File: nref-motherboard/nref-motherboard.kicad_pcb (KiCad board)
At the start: 2 copper layers, 110 x 80 mm, 137 parts, among them J1 POWSW, J10 Conn_01x20_Pin, J2 USB_C_Receptacle_USB2.0, J3 USBSEL, J4 1-2199230-6, J5 SYSCTL, J6 USB_INT1, J7 CHARGER, J8 Conn_01x12_Pin, J9 Conn_01x14_Pin, Q1 NTMFD6H840NL, Q2 NTMFD6H840NL, SW1 SW_DIP_x01, SW2 RESET, U1 reform2-som-connector, U2 74HC573, U3 MAX1837EUT33+T, U4 TLV1117-18, U5 TPS5450DDAR, U6 TPS5450DDAR, U7 LM2830XQMFE/NOPB, U8 RP2040, U9 W25Q32JVSS, Y1 12MHz 18pF

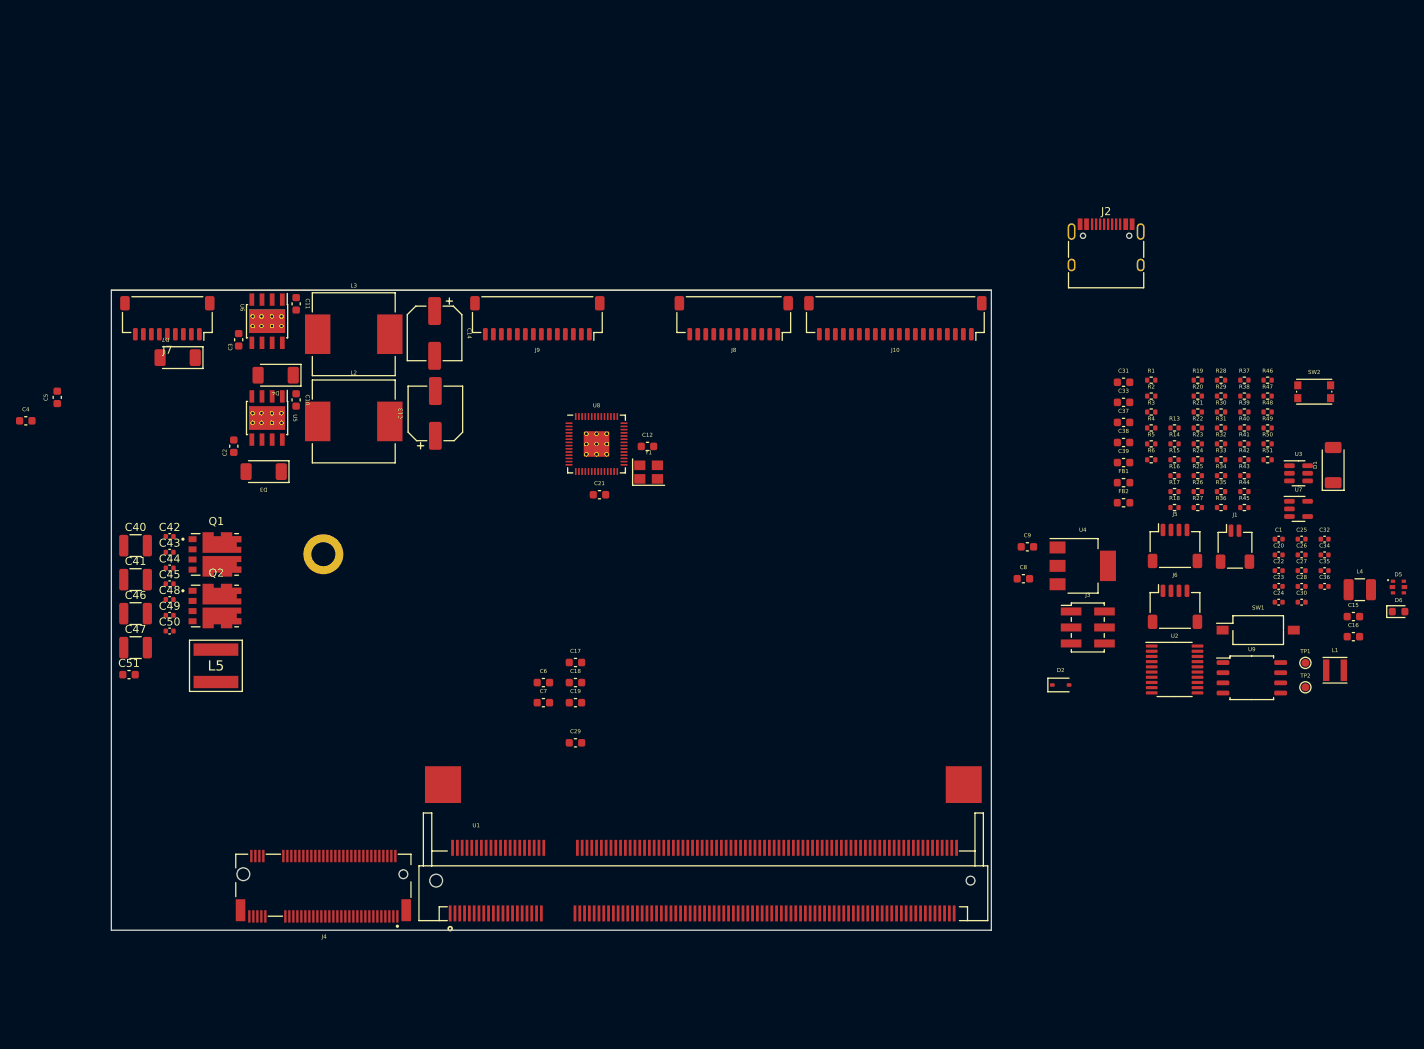
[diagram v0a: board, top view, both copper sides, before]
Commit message: motherboard: upgrade bucks to lm62460; some power layout
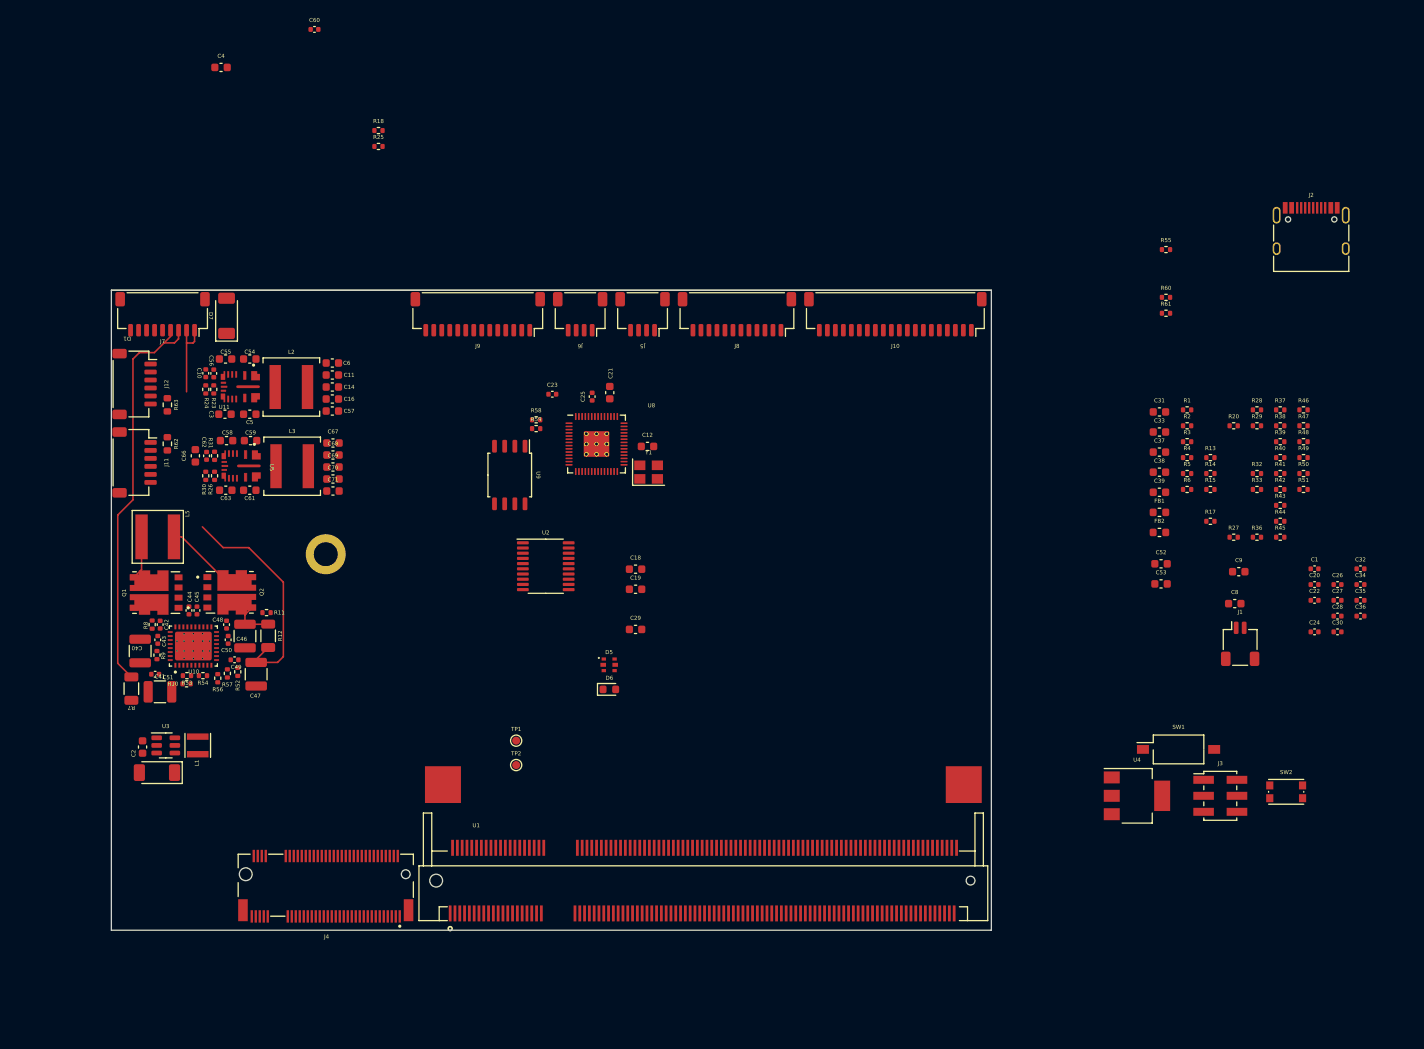
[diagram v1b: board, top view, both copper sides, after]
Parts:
- removed C13: 330uF, Capacitor_SMD:CP_Elec_6.3x5.4
- removed C15: 10nF, Capacitor_SMD:C_0603_1608Metric
- removed C17, C7: 22uF, Capacitor_SMD:C_0603_1608Metric
- removed D2: PMEG1020EA,115, Diode_SMD:D_SOD-323
- removed D3, D4: PMEG4050EP,115, Diode_SMD:D_SOD-128
- removed L4: 3.3uH, Inductor_SMD:L_1210_3225Metric
- removed R16, R34, R35: 0, Resistor_SMD:R_0402_1005Metric
- removed R19: 100k, Resistor_SMD:R_0402_1005Metric
- removed R21: 8.25k, Resistor_SMD:R_0402_1005Metric
- removed R22: 10k, Resistor_SMD:R_0402_1005Metric
- removed U6: TPS5450DDAR, Package_SO:TI_SO-PowerPAD-8_ThermalVias
- removed U7: LM2830XQMFE/NOPB, Package_TO_SOT_SMD:SOT-23-5
- added C52: 4.7uF, Capacitor_SMD:C_0603_1608Metric, F.Cu at (161.2, 134.2)
- added C53: 4.7uF, Capacitor_SMD:C_0603_1608Metric, F.Cu at (161.2, 136.7)
- added C54: 470nF, Capacitor_SMD:C_0603_1608Metric, F.Cu at (47.3, 108.6)
- added C55: 10uF, Capacitor_SMD:C_0603_1608Metric, F.Cu at (44.3, 108.6)
- added C56: 1uF, Capacitor_SMD:C_0402_1005Metric, F.Cu at (42.8, 110.4)
- added C57: 22uF, Capacitor_SMD:C_0603_1608Metric, F.Cu at (57.6, 115.1)
- added C58: 10uF, Capacitor_SMD:C_0603_1608Metric, F.Cu at (44.4, 118.8)
- added C59: 470nF, Capacitor_SMD:C_0603_1608Metric, F.Cu at (47.4, 118.8)
- added C60: 1uF, Capacitor_SMD:C_0402_1005Metric, F.Cu at (55.4, 67.4)
- added C61: 470nF, Capacitor_SMD:C_0603_1608Metric, F.Cu at (47.3, 125.0)
- added C62: 0.1uF, Capacitor_SMD:C_0402_1005Metric, F.Cu at (41.9, 120.7)
- added C63: 10uF, Capacitor_SMD:C_0603_1608Metric, F.Cu at (44.3, 125.0)
- added C66: 10pF, Capacitor_SMD:C_0603_1608Metric, F.Cu at (40.5, 120.7)
- added C67: 22uF, Capacitor_SMD:C_0603_1608Metric, F.Cu at (57.7, 119.1)
- added C68: 22uF, Capacitor_SMD:C_0603_1608Metric, F.Cu at (57.7, 120.6)
- added C69: 22uF, Capacitor_SMD:C_0603_1608Metric, F.Cu at (57.7, 122.1)
- added C70: 22uF, Capacitor_SMD:C_0603_1608Metric, F.Cu at (57.7, 123.6)
- added C71: 22uF, Capacitor_SMD:C_0603_1608Metric, F.Cu at (57.7, 125.1)
- added J11: BAT1, Connector_JST:JST_SH_SM06B-SRSS-TB_1x06-1MP_P1.00mm_Horizontal, F.Cu at (32.9, 121.5)
- added J12: BAT2, Connector_JST:JST_SH_SM06B-SRSS-TB_1x06-1MP_P1.00mm_Horizontal, F.Cu at (32.9, 111.7)
- added R10: 1M, Resistor_SMD:R_0402_1005Metric, F.Cu at (39.4, 149.2)
- added R11: 10, Resistor_SMD:R_0402_1005Metric, F.Cu at (49.4, 140.3)
- added R12: 5m, Resistor_SMD:R_1206_3216Metric, F.Cu at (49.6, 143.2)
- added R52: 10, Resistor_SMD:R_0402_1005Metric, F.Cu at (45.8, 147.7)
- added R53: 73.2k, Resistor_SMD:R_0402_1005Metric, F.Cu at (39.5, 148.2)
- added R54: 27.4k, Resistor_SMD:R_0402_1005Metric, F.Cu at (41.5, 148.2)
- added R55: 133k, Resistor_SMD:R_0402_1005Metric, F.Cu at (161.8, 94.9)
- added R56: 249k, Resistor_SMD:R_0402_1005Metric, F.Cu at (43.3, 148.5)
- added R57: 24.88k, Resistor_SMD:R_0402_1005Metric, F.Cu at (44.5, 147.9)
- added R58: R_Small, Resistor_SMD:R_0402_1005Metric, F.Cu at (83.1, 116.2)
- added R59: R_Small, Resistor_SMD:R_0402_1005Metric, F.Cu at (83.1, 117.3)
- added R60: 10k, Resistor_SMD:R_0402_1005Metric, F.Cu at (161.8, 100.9)
- added R61: 10, Resistor_SMD:R_0402_1005Metric, F.Cu at (161.8, 102.9)
- added R62: TODO, Resistor_SMD:R_0603_1608Metric, F.Cu at (37.0, 119.2)
- added R63: TODO, Resistor_SMD:R_0603_1608Metric, F.Cu at (37.0, 114.3)
- added R7: 5m, Resistor_SMD:R_1206_3216Metric, F.Cu at (32.5, 149.8)
- added R8: 10, Resistor_SMD:R_0402_1005Metric, F.Cu at (35.1, 141.8)
- added R9: 10, Resistor_SMD:R_0402_1005Metric, F.Cu at (35.7, 145.6)
- added U10: BQ25756RRVR, footprints:IC_BQ25756RRVR, F.Cu at (40.2, 144.5)
- added U11: LM62460, footprints:CONV_LM61495QRPHRQ1, F.Cu at (46.1, 112.1)
- C10: value 10nF -> 0.1uF; footprint Capacitor_SMD:C_0603_1608Metric -> Capacitor_SMD:C_0402_1005Metric
- C11, C16, C6: value 10nF -> 22uF
- C14: value 330uF -> 22uF; footprint Capacitor_SMD:CP_Elec_6.3x5.4 -> Capacitor_SMD:C_0603_1608Metric
- C4: value 10uF -> 10pF
- C5: value 10nF -> 470nF
- C51: footprint Capacitor_SMD:C_0603_1608Metric -> Capacitor_SMD:C_0402_1005Metric
- J7: value CHARGER -> PWR
- L2: value 15uH -> 2.7uH; footprint Inductor_SMD:L_Vishay_IHLP-4040 -> Inductor_SMD:L_Coilcraft_XAL6060-XXX
- L3: value 15uH -> 2.2uH; footprint Inductor_SMD:L_Vishay_IHLP-4040 -> Inductor_SMD:L_Coilcraft_XAL6060-XXX
- R18: value 100k -> 4.99k
- R23, R25: value 10k -> 100k
- R24: value 3.16k -> 24.9k
- R26: value 5.76k -> 100k
- R30: value 0 -> 43.2k
- R31: value 0 -> 4.99k
- U5: value TPS5450DDAR -> LM62460; footprint Package_SO:TI_SO-PowerPAD-8_ThermalVias -> footprints:CONV_LM61495QRPHRQ1
- moved D1 152.0 mm to (35.7, 160.3), turned to 180 degrees
- moved U3 145.6 mm to (36.8, 156.9)
- moved L1 142.5 mm to (40.8, 156.9), turned to 90 degrees
- moved C16 131.0 mm to (57.6, 113.6)
- moved R30 127.2 mm to (41.8, 123.2), turned to -90 degrees
- moved R31 125.9 mm to (42.9, 120.7), turned to -90 degrees
- moved R24 124.3 mm to (41.8, 112.4), turned to -90 degrees
- moved R23 123.2 mm to (42.8, 112.4), turned to 90 degrees
- moved R26 122.9 mm to (42.9, 123.2), turned to 90 degrees
- moved R25 110.4 mm to (63.4, 82.0)
- moved R18 110.1 mm to (63.4, 80.0)
- moved D6 99.1 mm to (92.2, 149.9)
- moved TP1 99.1 mm to (80.6, 156.3)
- moved TP2 99.1 mm to (80.6, 159.4)
- moved D5 99.1 mm to (92.2, 146.8)
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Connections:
- C10 pad 1: Net-(U5-BOOT) -> Net-(U11-CBOOT)
- C10 pad 2: Net-(D3-K) -> Net-(U11-SW)
- C11 pad 1: Net-(U6-BOOT) -> +5V
- C11 pad 2: Net-(D4-K) -> Net-(C11-Pad2)
- C14 pad 1: +3V3 -> +5V
- C14 pad 2: GND -> Net-(C11-Pad2)
- C16 pad 1: GND -> +5V
- C16 pad 2: +3V3 -> Net-(C11-Pad2)
- C4 pad 1: VCC -> Net-(U11-FB)
- C4 pad 2: GND -> Net-(C4-Pad2)
- C44 pad 1: Net-(Q1A-S1) -> /SW1
- C45 pad 2: Net-(Q2A-S1) -> /SW2
- C6 pad 1: VCC -> +5V
- C6 pad 2: GND -> Net-(C11-Pad2)
- J6 pad 2: USBH_3_DN -> USB2_DN
- J6 pad 3: USBH_3_DP -> USB2_DP
- L2 pad 1: Net-(D3-K) -> Net-(U11-SW)
- L3 pad 1: Net-(D4-K) -> Net-(U5-SW)
- L5 pad 1: Net-(Q1A-S1) -> /SW1
- L5 pad 2: Net-(Q2A-S1) -> /SW2
- Q1 pad 1: Net-(Q1A-S1) -> /SW1
- Q2 pad 1: Net-(Q2A-S1) -> GND
- Q2 pad 2: /HIDRV2 -> /LODRV2
- Q2 pad 3: GND -> /SW2
- Q2 pad 4: /LODRV2 -> /HIDRV2
- R17 pad 1: Net-(U2-Q0) -> Net-(U11-EN)
- R18 pad 1: Net-(U6-EN) -> +5V
- R18 pad 2: GND -> Net-(C4-Pad2)
- R23 pad 2: Net-(U5-VSENSE) -> Net-(U11-FB)
- R24 pad 1: Net-(U5-VSENSE) -> Net-(U11-FB)
- R25 pad 1: +3V3 -> Net-(U2-Q1)
- R25 pad 2: Net-(U6-VSENSE) -> GND
- R26 pad 1: Net-(U6-VSENSE) -> +3V3
- R26 pad 2: GND -> Net-(U5-FB)
- R30 pad 1: Net-(U8-GPIO8) -> Net-(U5-FB)
- R30 pad 2: LPC_MOSI -> GND
- R31 pad 1: Net-(U8-GPIO19) -> +3V3
- R31 pad 2: IMX_WAKE -> Net-(C66-Pad2)
- U2 pad 17: Net-(U2-Q2) -> unconnected-(U2-Q2-Pad17)
- U2 pad 18: unconnected-(U2-Q1-Pad18) -> Net-(U2-Q1)
- U2 pad 19: Net-(U2-Q0) -> Net-(U11-EN)
- U5 pad 1: Net-(U5-BOOT) -> GND
- U5 pad 2: unconnected-(U5-NC-Pad2) -> VCC
- U5 pad 3: unconnected-(U5-NC-Pad3) -> Net-(U5-CBOOT)
- U5 pad 4: Net-(U5-VSENSE) -> Net-(U5-CBOOT)
- U5 pad 5: Net-(U2-Q0) -> +3V3
- U5 pad 6: GND -> Net-(U5-RT)
- U5 pad 7: VCC -> Net-(U5-FB)
- U5 pad 8: Net-(D3-K) -> GND
- U5 pad 9: GND -> Net-(U5-RT)
- U8 pad 11: Net-(U8-GPIO8) -> LPC_MOSI
- U8 pad 14: Net-(U8-GPIO11) -> LPC_MISO
- U8 pad 30: Net-(U8-GPIO19) -> IMX_WAKE
- U8 pad 40: Net-(U8-GPIO28_ADC2) -> USB_SRC_EN
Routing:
- net VPD: track 0.00 -> 51.0 mm
- net VCC: track 0.00 -> 38.7 mm
- net /SW2: track 0.00 -> 11.8 mm
- net /SW1: track 0.00 -> 5.46 mm
- net Net-(C46-Pad1): track 0.00 -> 5.36 mm
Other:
- copper layers 2 -> 6

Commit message: motherboard: lots of connector shuffling and schematics
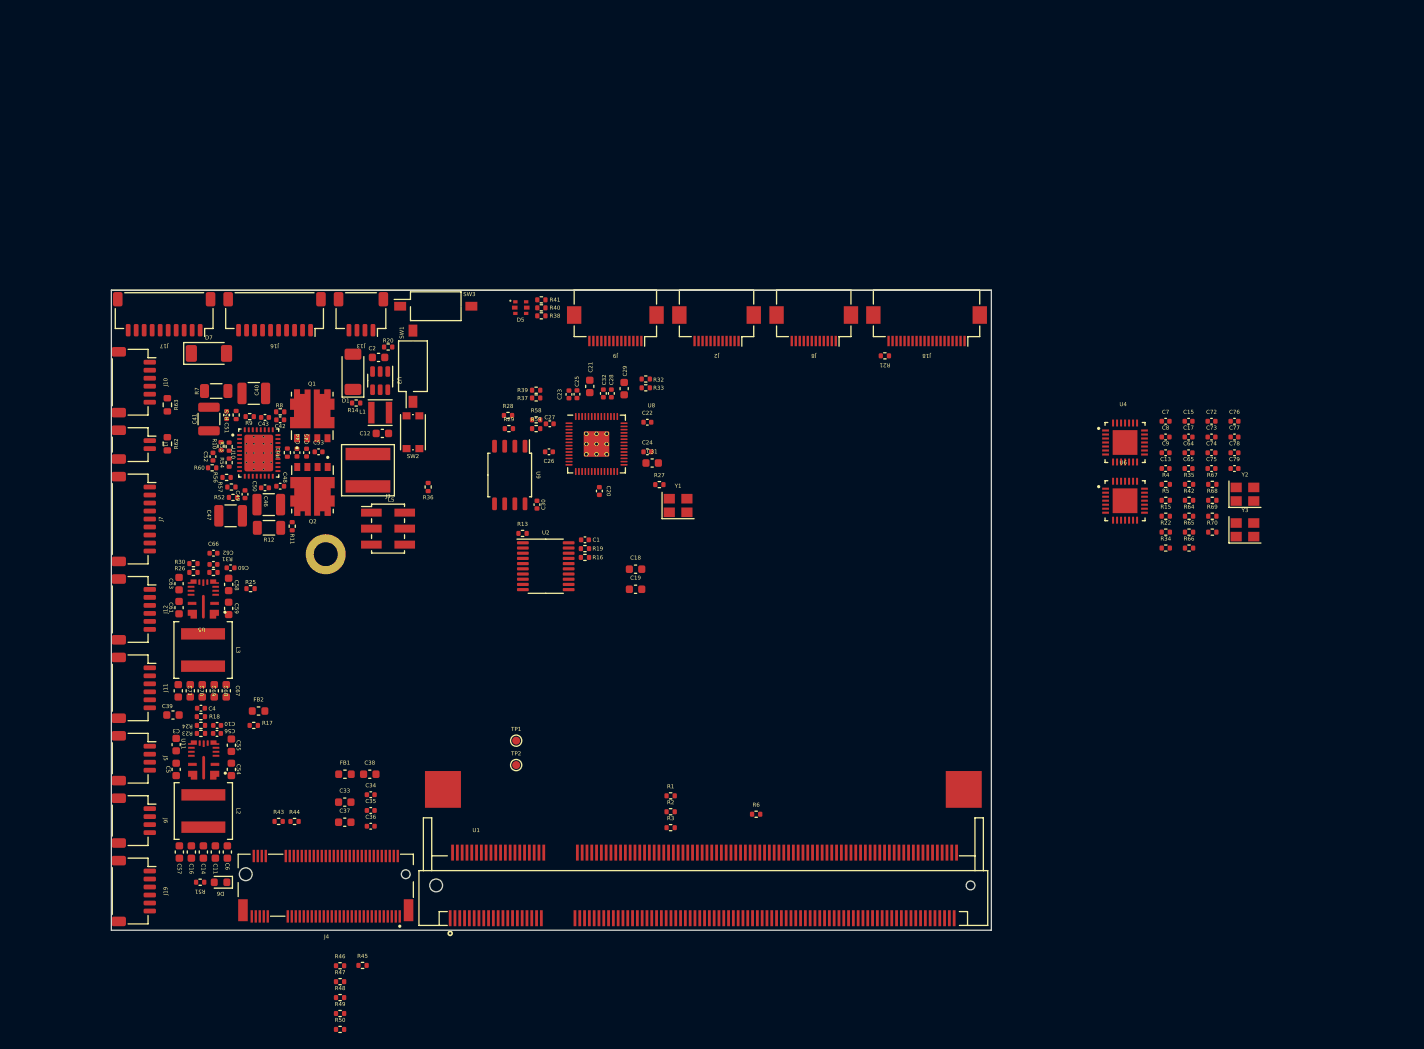
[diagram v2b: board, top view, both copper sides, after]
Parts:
- added C13: 0.1uF, Capacitor_SMD:C_0402_1005Metric, F.Cu at (161.8, 122.3)
- added C15: 0.1uF, Capacitor_SMD:C_0402_1005Metric, F.Cu at (164.7, 116.4)
- added C17: 0.1uF, Capacitor_SMD:C_0402_1005Metric, F.Cu at (164.7, 118.3)
- added C64: 0.1uF, Capacitor_SMD:C_0402_1005Metric, F.Cu at (164.7, 120.3)
- added C65: 0.1uF, Capacitor_SMD:C_0402_1005Metric, F.Cu at (164.7, 122.3)
- added C7: 18pF, Capacitor_SMD:C_0402_1005Metric, F.Cu at (161.8, 116.4)
- added C72: 18pF, Capacitor_SMD:C_0402_1005Metric, F.Cu at (167.5, 116.4)
- added C73: 18pF, Capacitor_SMD:C_0402_1005Metric, F.Cu at (167.5, 118.3)
- added C74: 0.1uF, Capacitor_SMD:C_0402_1005Metric, F.Cu at (167.5, 120.3)
- added C75: 0.1uF, Capacitor_SMD:C_0402_1005Metric, F.Cu at (167.5, 122.3)
- added C76: 0.1uF, Capacitor_SMD:C_0402_1005Metric, F.Cu at (170.4, 116.4)
- added C77: 0.1uF, Capacitor_SMD:C_0402_1005Metric, F.Cu at (170.4, 118.3)
- added C78: 0.1uF, Capacitor_SMD:C_0402_1005Metric, F.Cu at (170.4, 120.3)
- added C79: 0.1uF, Capacitor_SMD:C_0402_1005Metric, F.Cu at (170.4, 122.3)
- added J13: SYSCTL_USB, Connector_JST:JST_SH_SM04B-SRSS-TB_1x04-1MP_P1.00mm_Horizontal, F.Cu at (61.2, 103.0)
- added J16: Conn_01x10_Pin, Connector_JST:JST_SH_SM10B-SRSS-TB_1x10-1MP_P1.00mm_Horizontal, F.Cu at (50.4, 103.0)
- added J17: Conn_01x10_Pin, Connector_JST:JST_SH_SM10B-SRSS-TB_1x10-1MP_P1.00mm_Horizontal, F.Cu at (36.6, 103.0)
- added J18: Conn_01x20, Connector_FFC-FPC:Hirose_FH12-20S-0.5SH_1x20-1MP_P0.50mm_Horizontal, F.Cu at (131.9, 104.5)
- added J19: SER, Connector_JST:JST_SH_SM06B-SRSS-TB_1x06-1MP_P1.00mm_Horizontal, F.Cu at (32.8, 175.1)
- added R16: 1k, Resistor_SMD:R_0402_1005Metric, F.Cu at (89.2, 133.4)
- added R19: 1k, Resistor_SMD:R_0402_1005Metric, F.Cu at (89.2, 132.3)
- added R21: 0, Resistor_SMD:R_0402_1005Metric, F.Cu at (126.7, 108.2)
- added R22: 12k 1%, Resistor_SMD:R_0402_1005Metric, F.Cu at (161.8, 130.2)
- added R34: 1M, Resistor_SMD:R_0402_1005Metric, F.Cu at (161.8, 132.2)
- added R35: 50k, Resistor_SMD:R_0402_1005Metric, F.Cu at (164.7, 124.3)
- added R64: 50k, Resistor_SMD:R_0402_1005Metric, F.Cu at (164.7, 128.2)
- added R65: 50k, Resistor_SMD:R_0402_1005Metric, F.Cu at (164.7, 130.2)
- added R66: 0, Resistor_SMD:R_0402_1005Metric, F.Cu at (164.7, 132.2)
- added R67: 12k 1%, Resistor_SMD:R_0402_1005Metric, F.Cu at (167.6, 124.3)
- added R68: 1M, Resistor_SMD:R_0402_1005Metric, F.Cu at (167.6, 126.3)
- added R69: 50k, Resistor_SMD:R_0402_1005Metric, F.Cu at (167.6, 128.2)
- added R70: 0, Resistor_SMD:R_0402_1005Metric, F.Cu at (167.6, 130.2)
- added SW3: SW_DIP_x01, Button_Switch_SMD:SW_DIP_SPSTx01_Slide_Omron_A6S-110x_W8.9mm_P2.54mm, F.Cu at (70.5, 102.0)
- added U6: USB2412-DZK, footprints:QFN50P500X500X100-29N, F.Cu at (156.7, 126.3)
- added Y2: 24MHz, Crystal:Crystal_SMD_3225-4Pin_3.2x2.5mm, F.Cu at (171.7, 125.5)
- added Y3: 24MHz, Crystal:Crystal_SMD_3225-4Pin_3.2x2.5mm, F.Cu at (171.7, 129.9)
- C4, C52, C53, C66: footprint Capacitor_SMD:C_0603_1608Metric -> Capacitor_SMD:C_0402_1005Metric
- C8: value 1uF -> 18pF; footprint Capacitor_SMD:C_0603_1608Metric -> Capacitor_SMD:C_0402_1005Metric
- C9: value 1uF -> 0.1uF; footprint Capacitor_SMD:C_0603_1608Metric -> Capacitor_SMD:C_0402_1005Metric
- J10: value Conn_01x20_Pin -> DISP; footprint Connector_JST:JST_SH_SM20B-SRSS-TB_1x20-1MP_P1.00mm_Horizontal -> Connector_JST:JST_SH_SM06B-SRSS-TB_1x06-1MP_P1.00mm_Horizontal
- J2: value USB_C_Receptacle_USB2.0 -> Conn_01x12_Pin; footprint Connector_USB:USB_C_Receptacle_HRO_TYPE-C-31-M-12 -> Connector_FFC-FPC:Hirose_FH12-12S-0.5SH_1x12-1MP_P0.50mm_Horizontal
- J8: footprint Connector_JST:JST_SH_SM12B-SRSS-TB_1x12-1MP_P1.00mm_Horizontal -> Connector_FFC-FPC:Hirose_FH12-12S-0.5SH_1x12-1MP_P0.50mm_Horizontal
- J9: footprint Connector_JST:JST_SH_SM14B-SRSS-TB_1x14-1MP_P1.00mm_Horizontal -> Connector_FFC-FPC:Hirose_FH12-14S-0.5SH_1x14-1MP_P0.50mm_Horizontal
- R4, R5: value 0 -> 50k
- R42: value DNP -> 0
- U4: value TLV1117-18 -> USB2412-DZK; footprint Package_TO_SOT_SMD:SOT-223 -> footprints:QFN50P500X500X100-29N
- moved R51 146.4 mm to (41.1, 174.0), turned to 180 degrees
- moved J1 140.5 mm to (32.8, 119.3), turned to -90 degrees
- moved R46 139.0 mm to (58.6, 184.4)
- moved R47 139.0 mm to (58.6, 186.4)
- moved R48 139.0 mm to (58.6, 188.4)
- moved R49 139.0 mm to (58.6, 190.4)
- moved R50 139.0 mm to (58.6, 192.4)
- moved R43 131.3 mm to (50.9, 166.4)
- moved R44 128.8 mm to (52.9, 166.4)
- moved R45 126.6 mm to (61.4, 184.4)
- moved C34 126.5 mm to (62.4, 163.1)
- moved C35 126.5 mm to (62.4, 165.0)
- moved C36 126.5 mm to (62.4, 167.0)
- moved C39 126.4 mm to (37.7, 153.1)
- moved R17 122.3 mm to (47.8, 154.4)
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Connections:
- C8 pad 1: Net-(U4-VI) -> Net-(U4-XTALIN/CLKIN)
- C9 pad 1: +1V8 -> Net-(U4-CRFILT)
- J10 pad 1: GND -> +5V
- J10 pad 2: HDMI_HPD -> +3V3
- J10 pad 3: HDMI_CEC -> GND
- J10 pad 4: HDMI_SCL -> BACKLIGHT_EN
- J10 pad 5: HDMI_SDA -> BACKLIGHT_PWM
- J3 pad 1: USB2_DN -> USB2B_DN
- J3 pad 2: USB2_DP -> USB2B_DP
- J6 pad 2: USB2_DN -> USB1B_DN
- J6 pad 3: USB2_DP -> USB1B_DP
- J8 pad 11: USB1_DP -> USB1A_DP
- J8 pad 12: USB1_DN -> USB1A_DN
- R15 pad 1: Net-(U4-VI) -> USB_HUB_RESET
- R15 pad 2: +3V3 -> Net-(U4-~{RESET_IN})
- R17 pad 1: Net-(U11-EN) -> 5V_ENABLE_L
- R25 pad 1: Net-(U2-Q1) -> 3V3_ENABLE_L
- R4 pad 1: RP_UART2_RX -> GND
- R4 pad 2: Net-(U1-UART3_TXD) -> Net-(U4-HS_IND)
- R42 pad 1: Net-(J2-VBUS-PadA4) -> Net-(U4-VBUS_DET)
- R42 pad 2: +5V -> +3V3
- R5 pad 1: Net-(U1-UART3_RXD) -> GND
- R5 pad 2: RP_UART2_TX -> Net-(U4-NON_REM1)
- U1 pad 164: unconnected-(U1-SPDIF_RX/PWM2-Pad164) -> BACKLIGHT_PWM
- U1 pad 30: Net-(U1-UART3_TXD) -> RP_UART2_RX
- U1 pad 32: Net-(U1-UART3_RXD) -> RP_UART2_TX
- U11 pad 13: Net-(U11-EN) -> 5V_ENABLE_L
- U2 pad 15: DISP_EN_L -> unconnected-(U2-Q4-Pad15)
- U2 pad 16: ~{DISP_RESET_L} -> unconnected-(U2-Q3-Pad16)
- U2 pad 19: Net-(U11-EN) -> Net-(U2-Q0)
- U2 pad 4: 1V1_ENABLE -> unconnected-(U2-D2-Pad4)
- U2 pad 5: ~{DISP_RESET} -> unconnected-(U2-D3-Pad5)
- U2 pad 6: DISP_EN -> unconnected-(U2-D4-Pad6)
- U4 pad 1: GND -> USB2A_DP
- U4 pad 2: +1V8 -> USB2B_DN
- U4 pad 3: Net-(U4-VI) -> USB2B_DP
- U4 pad 4: +1V8 -> +3V3
- U5 pad 13: Net-(U2-Q1) -> 3V3_ENABLE_L
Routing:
- net VPD: track 51.0 -> 0.00 mm
- net VCC: track 38.7 -> 0.00 mm
- net /SW2: track 11.8 -> 0.00 mm
- net /SW1: track 5.46 -> 0.00 mm
- net Net-(C46-Pad1): track 5.36 -> 0.00 mm
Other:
- board text removed: "{dblquote}big{dblquote} zone"
